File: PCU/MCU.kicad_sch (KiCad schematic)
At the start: 18 parts, among them IC5 STM32G473CCT3, Y1 ECS-80-10-30B-CWN-TR

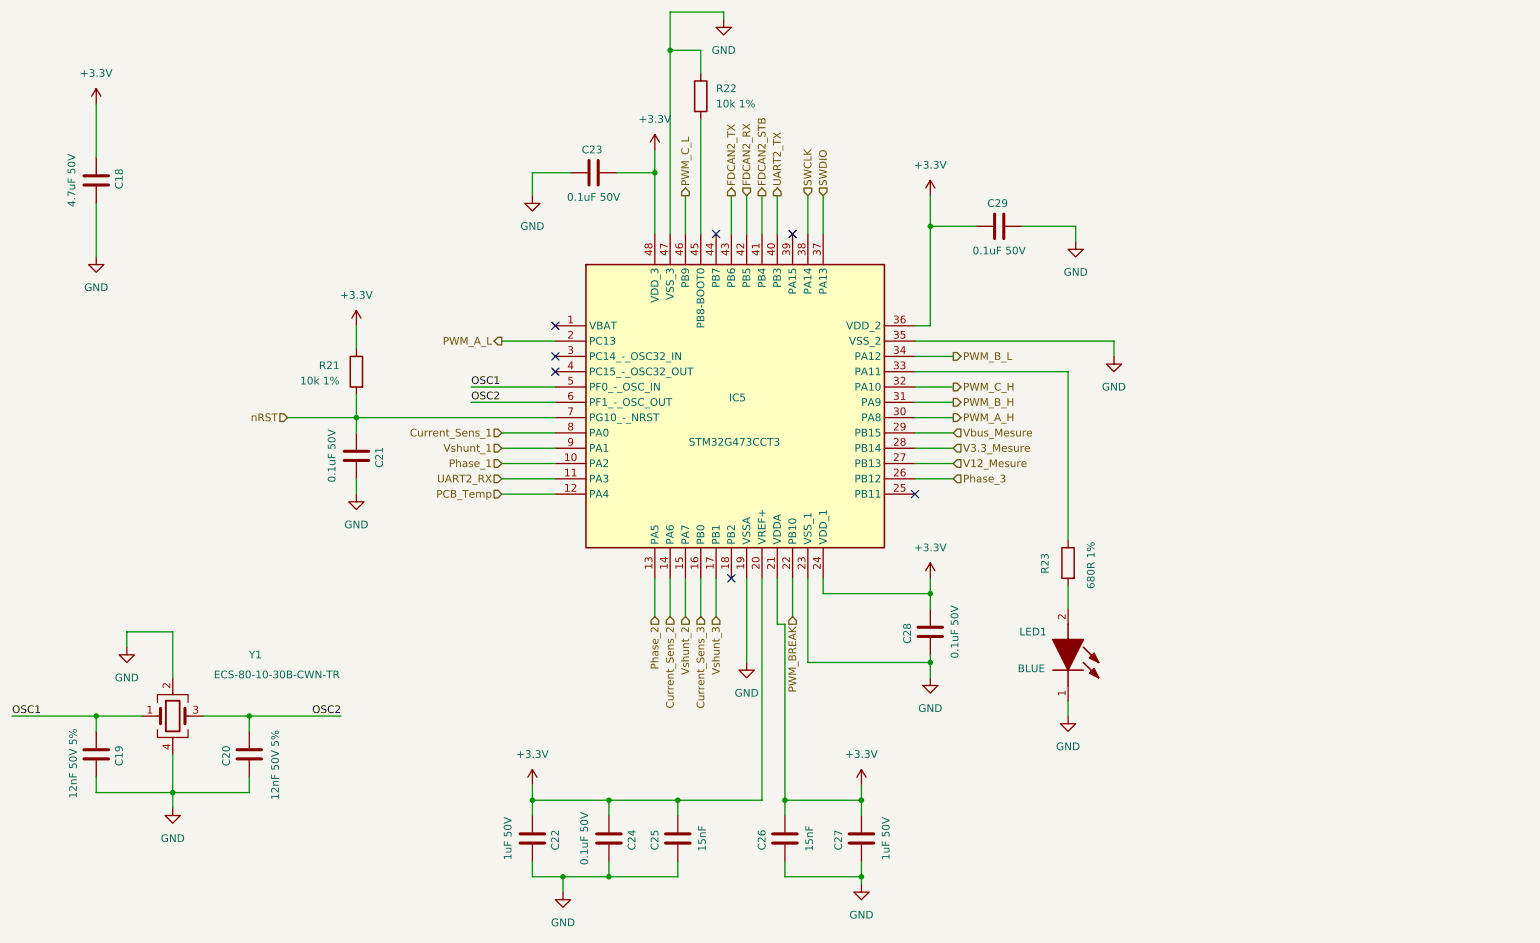
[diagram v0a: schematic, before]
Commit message: ESC Block Updated
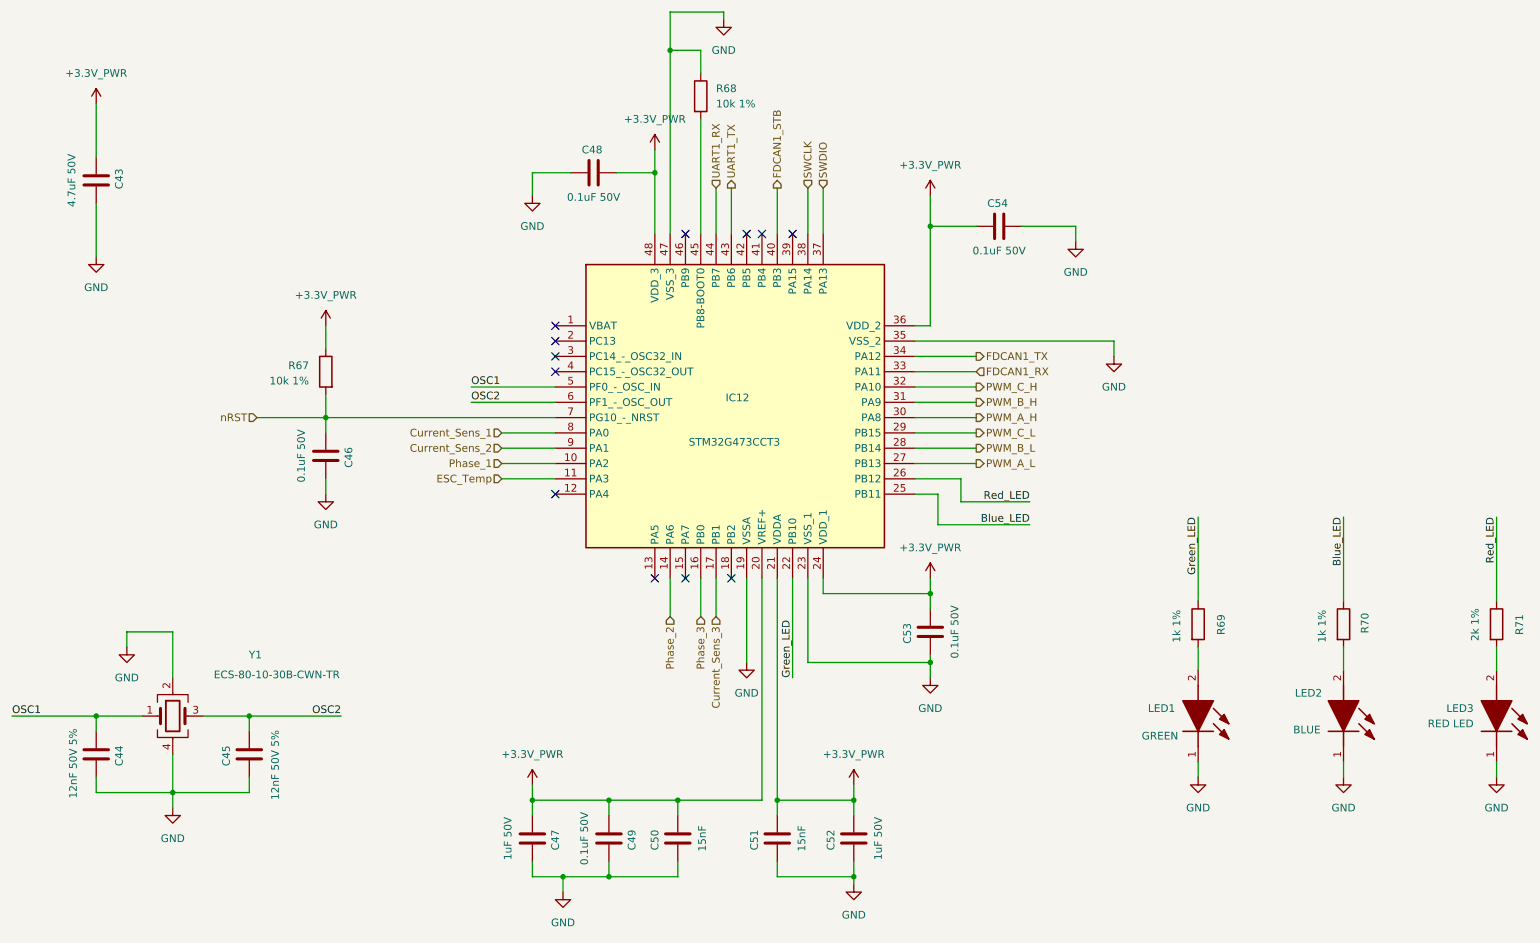
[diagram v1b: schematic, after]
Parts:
- added LED1: GREEN, BassinaLib_LEDs:LEDM168X80N, symbol BassinaLib_LEDs:APHD1608LZGCK
- added LED3: RED LED, BassinaLib_LEDs:LEDM168X80N, symbol BassinaLib_LEDs:APHD1608LSURCK
- added R69: 1k 1%, Resistor_SMD:R_0603_1608Metric, symbol Device:R
- added R71: 2k 1%, Resistor_SMD:R_0603_1608Metric, symbol Device:R
- R70: renamed from R23; value 680R 1% -> 1k 1%; Manufacturer_Part_Number RC0603FR-07680RL -> RT0603FRE071KL
- renumbered C18 to C43, C19 to C44, C20 to C45, C21 to C46, C22 to C47, C23 to C48, C24 to C49, C25 to C50, C26 to C51, C27 to C52, C28 to C53, C29 to C54, IC5 to IC12, LED1 to LED2, R21 to R67, R22 to R68
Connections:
- net V12_Mesure is gone; now on net PWM_A_L: IC12.27 (PB13)
- net V3.3_Mesure is gone; now on net PWM_B_L: IC12.28 (PB14)
- net Vbus_Mesure is gone; now on net PWM_C_L: IC12.29 (PB15)
- net Vshunt_1 is gone; now on net Current_Sens_2: IC12.9 (PA1)
- net Vshunt_3 is gone; now on net Current_Sens_3: IC12.17 (PB1)
- net Current_Sens_2: no longer IC12.14 (PA6)
- net Current_Sens_3: no longer IC12.16 (PB0)
- net GND: now also LED1.1 (K), LED3.1 (K)
- net PWM_A_L: no longer IC12.2 (PC13)
- net PWM_B_L: no longer IC12.34 (PA12)
- net PWM_C_L: no longer IC12.46 (PB9)
- net Phase_2: now also IC12.14 (PA6); no longer IC12.13 (PA5)
- net Phase_3: now also IC12.16 (PB0); no longer IC12.26 (PB12)
- net Blue_LED: now reaches R70.1
- net Blue_LED: now also IC12.25 (PB11); no longer IC12.33 (PA11)
- net UART1_RX: now reaches IC12.44 (PB7)
- net +3.3V renamed +3.3V_PWR
- net FDCAN2_RX: no longer names the net of IC12.42 (PB5)
- net FDCAN2_STB: no longer names the net of IC12.41 (PB4)
- net FDCAN2_TX renamed UART1_TX
- net PCB_Temp: no longer names the net of IC12.12 (PA4)
- net PWM_BREAK renamed Green_LED
- net Green_LED: now also R69.1
- net UART2_RX renamed ESC_Temp
- net UART2_TX renamed FDCAN1_STB
- net Vshunt_2: no longer names the net of IC12.15 (PA7)
- new net: LED3.2 (A), R71.2
- new net: LED1.2 (A), R69.2
- new net FDCAN1_RX: IC12.33 (PA11)
- new net FDCAN1_TX: IC12.34 (PA12)
- new net Red_LED: IC12.26 (PB12), R71.1
- no-connect marks 7 -> 12
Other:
- moved on the sheet: C46, C51, C52, LED2, R67, R70

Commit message: high power supply block
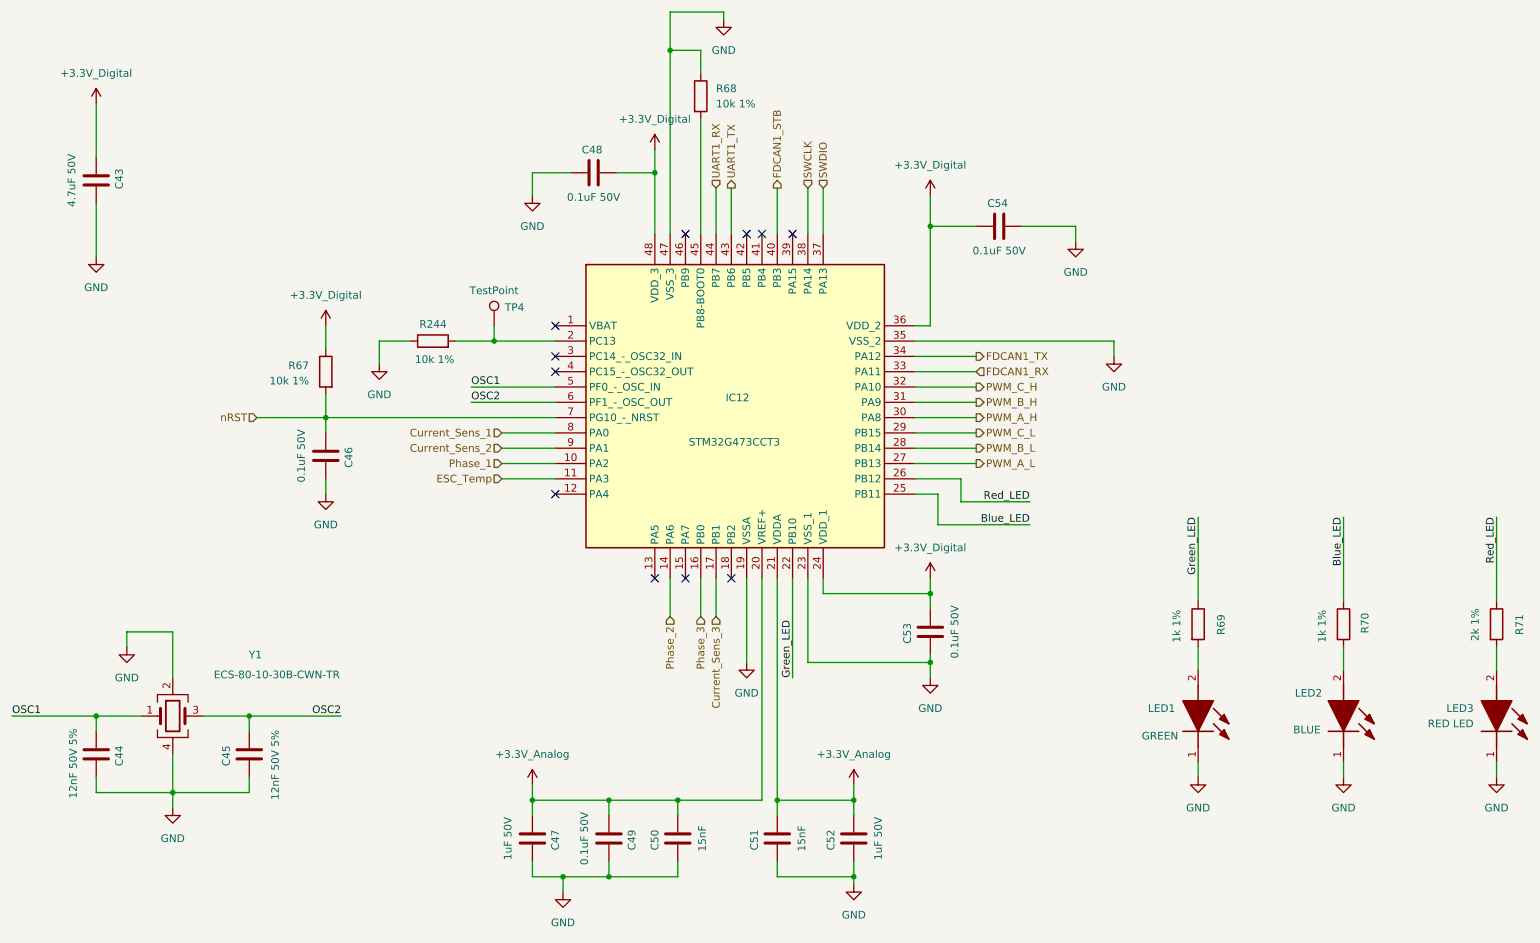
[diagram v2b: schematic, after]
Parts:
- added R244: 10k 1%, Resistor_SMD:R_0603_1608Metric, symbol Device:R
- added TP4: TestPoint, TestPoint:TestPoint_Pad_D1.0mm, symbol Connector:TestPoint
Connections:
- net GND: now also R244.1
- net at IC12.2 (PC13): now also R244.2, TP4.1
- net +3.3V_PWR renamed +3.3V_Digital
- net +3.3V_Digital: no longer C47.2, C49.2, C50.2, C51.2, C52.2, IC12.20 (VREF+), IC12.21 (VDDA)
- new net +3.3V_Analog: C47.2, C49.2, C50.2, C51.2, C52.2, IC12.20 (VREF+), IC12.21 (VDDA)
- no-connect marks 12 -> 11

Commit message: Supervisor Block
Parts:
- renumbered C43 to C49, C44 to C50, C45 to C51, C46 to C52, C47 to C53, C48 to C54, C49 to C55, C50 to C56, C51 to C57, C52 to C58, C53 to C59, C54 to C60, R244 to R68, R68 to R69, R69 to R70, R70 to R71, R71 to R72, TP4 to TP1

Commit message: Analog Signal Routing started
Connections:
- net Current_Sens_1: now also IC12.9 (PA1); no longer IC12.8 (PA0)
- net Current_Sens_2: now also IC12.17 (PB1); no longer IC12.9 (PA1)
- net Current_Sens_3: now also IC12.8 (PA0); no longer IC12.17 (PB1)
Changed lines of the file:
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@@
 		)
 	)
-	(hierarchical_label "Current_Sens_3"
+	(hierarchical_label "Current_Sens_2"
 		(shape input)
 		(at 140.97 120.65 270)
@@
 		)
 	)
-	(hierarchical_label "Current_Sens_2"
+	(hierarchical_label "Current_Sens_1"
 		(shape input)
 		(at 105.41 92.71 180)
@@
 		)
 	)
-	(hierarchical_label "Current_Sens_1"
+	(hierarchical_label "Current_Sens_3"
 		(shape input)
 		(at 105.41 90.17 180)

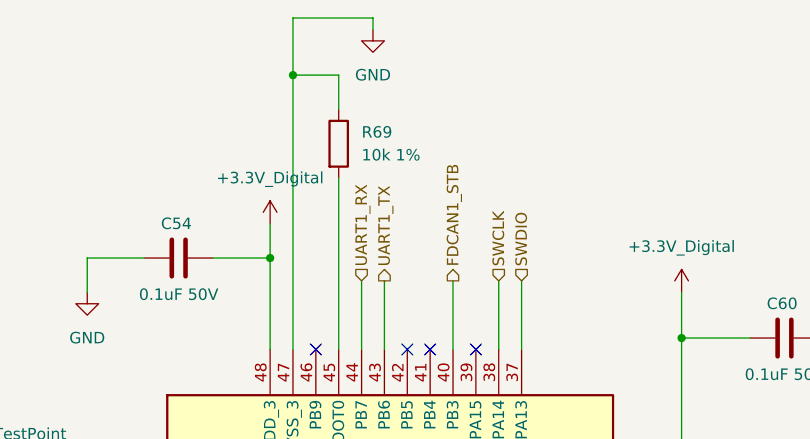
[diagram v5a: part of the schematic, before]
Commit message: ESCs Analog signals routed
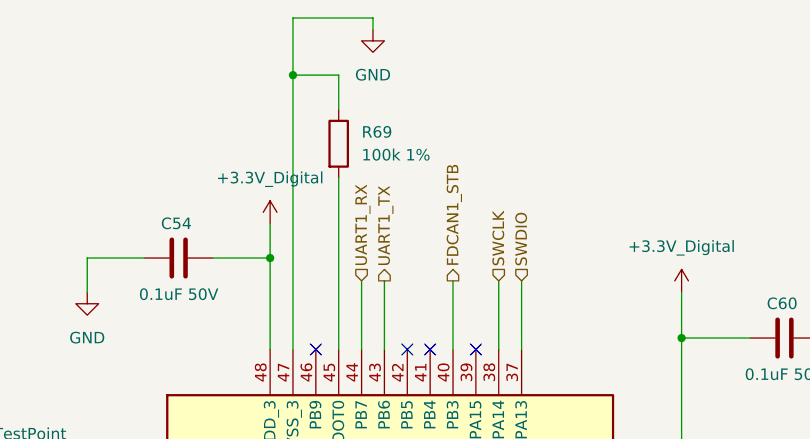
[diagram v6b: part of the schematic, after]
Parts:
- R69: value 10k 1% -> 100k 1%; Manufacturer_Part_Number AF0603FR-0710KL -> AT0603FRE07100KL
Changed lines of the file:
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@@
 			)
 		)
-		(property "Value" "10k 1%"
+		(property "Value" "100k 1%"
 			(at 140.97 35.5599 0)
 			(effects
@@
 			)
 		)
-		(property "Manufacturer_Part_Number" "AF0603FR-0710KL"
+		(property "Manufacturer_Part_Number" "AT0603FRE07100KL"
 			(at 138.43 34.29 0)
 			(effects

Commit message: Components library added
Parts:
- TP1: now left out of the parts list
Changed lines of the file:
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@@
 		(unit 1)
 		(exclude_from_sim no)
-		(in_bom yes)
+		(in_bom no)
 		(on_board yes)
 		(dnp no)

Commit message: Fly controller design started
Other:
- company: BASSINGA Lab -> BASSINGA_LAB
- title: (none) -> Propulsion Control Unit
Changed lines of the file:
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@@
 	(paper "A4")
 	(title_block
+		(title "Propulsion Control Unit")
 		(date "2025-05-21")
 		(rev "v1.0")
-		(company "BASSINGA Lab")
+		(company "BASSINGA_LAB")
+		(comment 1 "Copyright © 2025 Andresse Brisel BASSINGA ")
 	)
 	(junction
